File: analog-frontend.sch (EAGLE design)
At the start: 2 parts

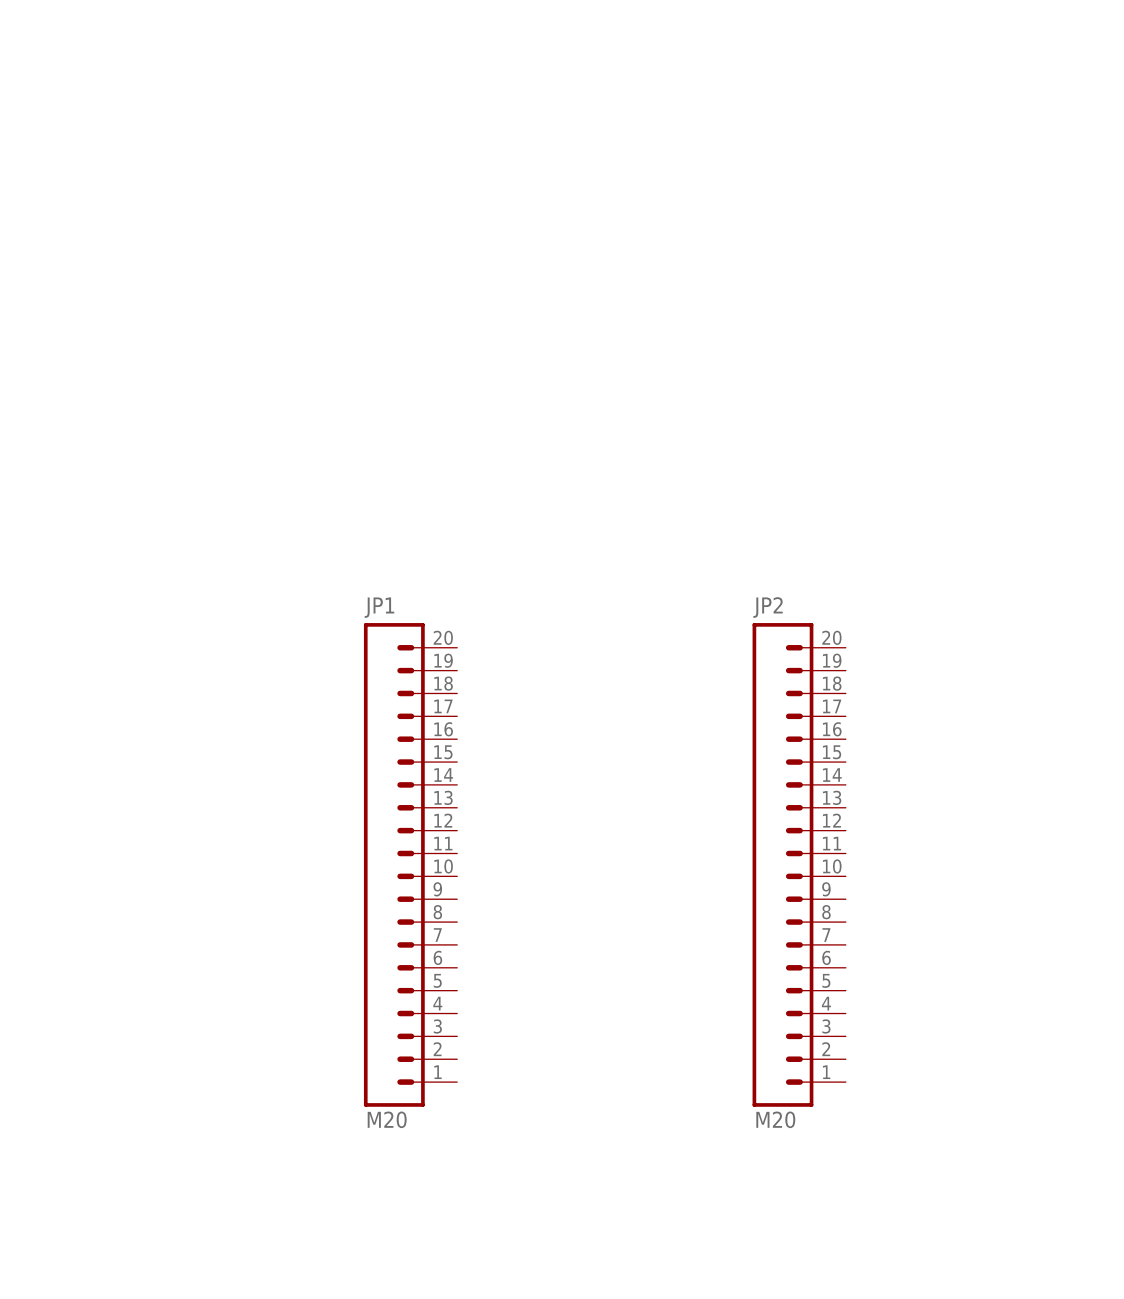
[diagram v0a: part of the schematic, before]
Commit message: added analog mux
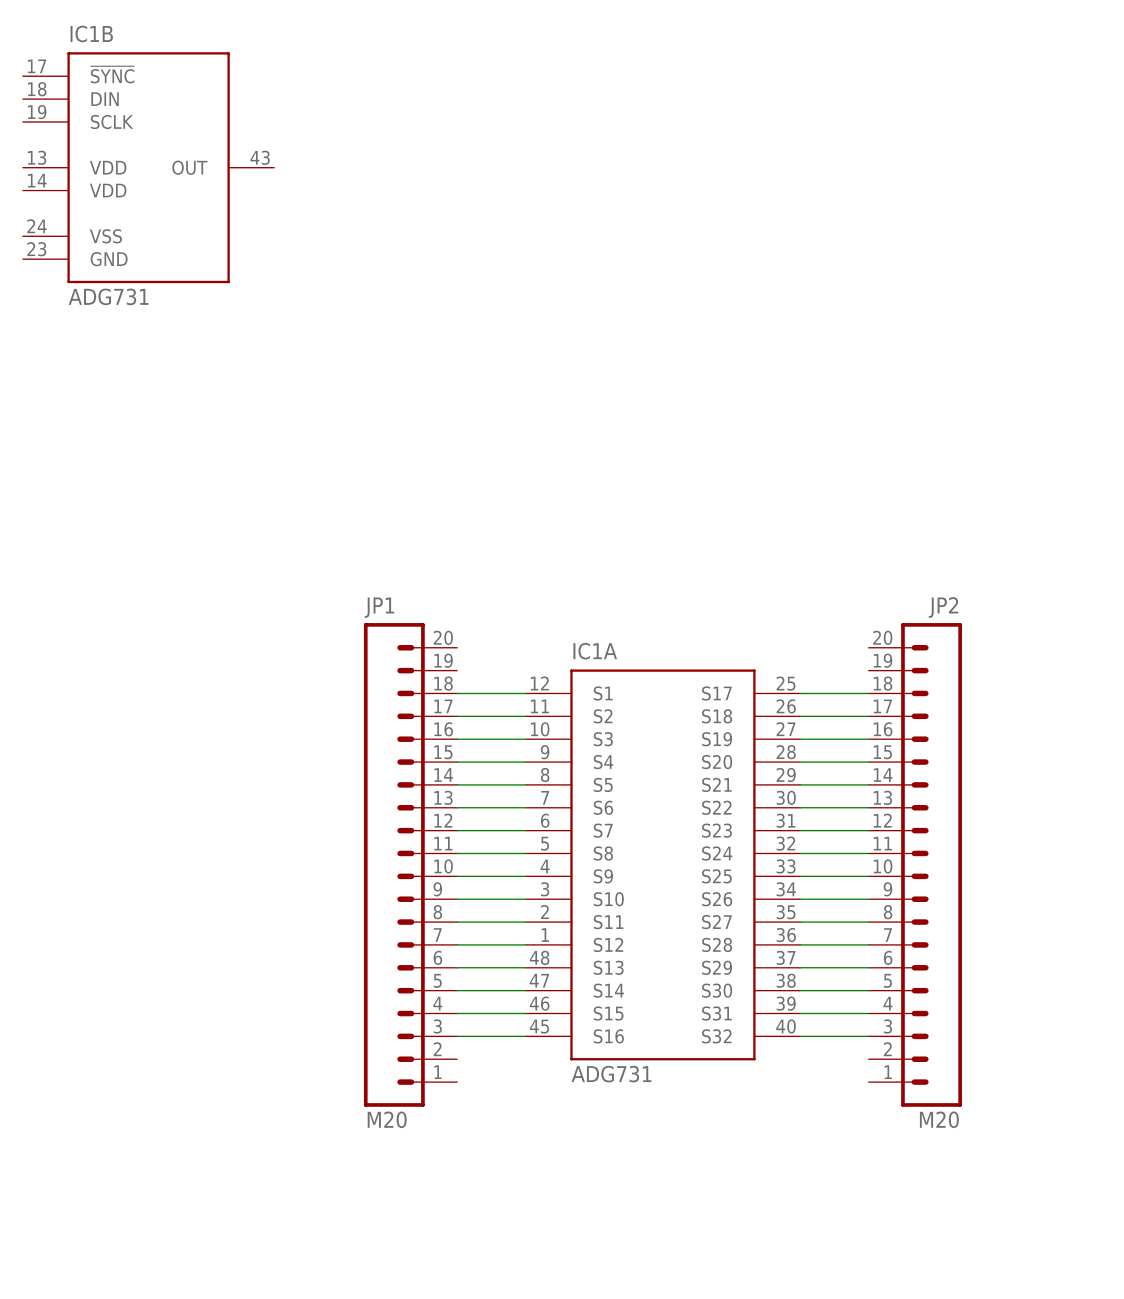
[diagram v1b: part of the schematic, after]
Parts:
- added IC1: ADG731, mor307:ADG731
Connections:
- new net N$1: IC1A.S1, JP1.18
- new net N$10: IC1A.S7, JP1.12
- new net N$11: IC1A.S8, JP1.11
- new net N$12: IC1A.S9, JP1.10
- new net N$13: IC1A.S10, JP1.9
- new net N$14: IC1A.S11, JP1.8
- new net N$15: IC1A.S12, JP1.7
- new net N$16: IC1A.S13, JP1.6
- new net N$17: IC1A.S14, JP1.5
- new net N$18: IC1A.S15, JP1.4
- new net N$19: IC1A.S18, JP2.17
- new net N$2: IC1A.S16, JP1.3
- new net N$20: IC1A.S19, JP2.16
- new net N$21: IC1A.S20, JP2.15
- new net N$22: IC1A.S21, JP2.14
- new net N$23: IC1A.S22, JP2.13
- new net N$24: IC1A.S23, JP2.12
- new net N$25: IC1A.S24, JP2.11
- new net N$26: IC1A.S25, JP2.10
- new net N$27: IC1A.S26, JP2.9
- new net N$28: IC1A.S27, JP2.8
- new net N$29: IC1A.S28, JP2.7
- new net N$3: IC1A.S17, JP2.18
- new net N$30: IC1A.S29, JP2.6
- new net N$31: IC1A.S30, JP2.5
- new net N$32: IC1A.S31, JP2.4
- new net N$4: IC1A.S32, JP2.3
- new net N$5: IC1A.S2, JP1.17
- new net N$6: IC1A.S3, JP1.16
- new net N$7: IC1A.S4, JP1.15
- new net N$8: IC1A.S5, JP1.14
- new net N$9: IC1A.S6, JP1.13
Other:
- moved on the sheet: JP2
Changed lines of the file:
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@@
 <part name="JP1" library="mor307" deviceset="M20" device=""/>
 <part name="JP2" library="mor307" deviceset="M20" device=""/>
+<part name="IC1" library="mor307" deviceset="ADG731" device=""/>
 </parts>
 <sheets>
@@
 </instance>
 <instance part="JP1" gate="G$1" x="73.66" y="144.78"/>
-<instance part="JP2" gate="G$1" x="116.84" y="144.78"/>
+<instance part="JP2" gate="G$1" x="139.7" y="144.78" rot="MR0"/>
+<instance part="IC1" gate="B" x="48.26" y="220.98"/>
+<instance part="IC1" gate="A" x="106.68" y="142.24"/>
 </instances>
 <busses>
 </busses>
 <nets>
+<net name="N$1" class="0">
+<segment>
+<pinref part="IC1" gate="A" pin="S1"/>
+<pinref part="JP1" gate="G$1" pin="18"/>
+<wire x1="91.44" y1="162.56" x2="83.82" y2="162.56" width="0.1524" layer="91"/>
+</segment>
+</net>
+<net name="N$2" class="0">
+<segment>
+<pinref part="IC1" gate="A" pin="S16"/>
+<pinref part="JP1" gate="G$1" pin="3"/>
+<wire x1="91.44" y1="124.46" x2="83.82" y2="124.46" width="0.1524" layer="91"/>
+</segment>
+</net>
+<net name="N$3" class="0">
+<segment>
+<pinref part="IC1" gate="A" pin="S17"/>
+<pinref part="JP2" gate="G$1" pin="18"/>
+<wire x1="121.92" y1="162.56" x2="129.54" y2="162.56" width="0.1524" layer="91"/>
+</segment>
+</net>
+<net name="N$4" class="0">
+<segment>
+<pinref part="IC1" gate="A" pin="S32"/>
+<pinref part="JP2" gate="G$1" pin="3"/>
+<wire x1="121.92" y1="124.46" x2="129.54" y2="124.46" width="0.1524" layer="91"/>
+</segment>
+</net>
+<net name="N$5" class="0">
+<segment>
+<pinref part="IC1" gate="A" pin="S2"/>
+<pinref part="JP1" gate="G$1" pin="17"/>
+<wire x1="91.44" y1="160.02" x2="83.82" y2="160.02" width="0.1524" layer="91"/>
+</segment>
+</net>
+<net name="N$6" class="0">
+<segment>
+<pinref part="IC1" gate="A" pin="S3"/>
+<pinref part="JP1" gate="G$1" pin="16"/>
+<wire x1="91.44" y1="157.48" x2="83.82" y2="157.48" width="0.1524" layer="91"/>
+</segment>
+</net>
+<net name="N$7" class="0">
+<segment>
+<pinref part="IC1" gate="A" pin="S4"/>
+<pinref part="JP1" gate="G$1" pin="15"/>
+<wire x1="91.44" y1="154.94" x2="83.82" y2="154.94" width="0.1524" layer="91"/>
+</segment>
+</net>
+<net name="N$8" class="0">
+<segment>
+<pinref part="IC1" gate="A" pin="S5"/>
+<pinref part="JP1" gate="G$1" pin="14"/>
+<wire x1="91.44" y1="152.4" x2="83.82" y2="152.4" width="0.1524" layer="91"/>
+</segment>
+</net>
+<net name="N$9" class="0">
+<segment>
+<pinref part="IC1" gate="A" pin="S6"/>
+<pinref part="JP1" gate="G$1" pin="13"/>
+<wire x1="91.44" y1="149.86" x2="83.82" y2="149.86" width="0.1524" layer="91"/>
+</segment>
+</net>
+<net name="N$10" class="0">
+<segment>
+<pinref part="IC1" gate="A" pin="S7"/>
+<pinref part="JP1" gate="G$1" pin="12"/>
+<wire x1="91.44" y1="147.32" x2="83.82" y2="147.32" width="0.1524" layer="91"/>
+</segment>
+</net>
+<net name="N$11" class="0">
+<segment>
+<pinref part="IC1" gate="A" pin="S8"/>
+<pinref part="JP1" gate="G$1" pin="11"/>
+<wire x1="91.44" y1="144.78" x2="83.82" y2="144.78" width="0.1524" layer="91"/>
+</segment>
+</net>
+<net name="N$12" class="0">
+<segment>
+<pinref part="IC1" gate="A" pin="S9"/>
+<pinref part="JP1" gate="G$1" pin="10"/>
+<wire x1="91.44" y1="142.24" x2="83.82" y2="142.24" width="0.1524" layer="91"/>
+</segment>
+</net>
+<net name="N$13" class="0">
+<segment>
+<pinref part="IC1" gate="A" pin="S10"/>
+<pinref part="JP1" gate="G$1" pin="9"/>
+<wire x1="91.44" y1="139.7" x2="83.82" y2="139.7" width="0.1524" layer="91"/>
+</segment>
+</net>
+<net name="N$14" class="0">
+<segment>
+<pinref part="IC1" gate="A" pin="S11"/>
+<pinref part="JP1" gate="G$1" pin="8"/>
+<wire x1="91.44" y1="137.16" x2="83.82" y2="137.16" width="0.1524" layer="91"/>
+</segment>
+</net>
+<net name="N$15" class="0">
+<segment>
+<pinref part="IC1" gate="A" pin="S12"/>
+<pinref part="JP1" gate="G$1" pin="7"/>
+<wire x1="91.44" y1="134.62" x2="83.82" y2="134.62" width="0.1524" layer="91"/>
+</segment>
+</net>
+<net name="N$16" class="0">
+<segment>
+<pinref part="IC1" gate="A" pin="S13"/>
+<pinref part="JP1" gate="G$1" pin="6"/>
+<wire x1="91.44" y1="132.08" x2="83.82" y2="132.08" width="0.1524" layer="91"/>
+</segment>
+</net>
+<net name="N$17" class="0">
+<segment>
+<pinref part="IC1" gate="A" pin="S14"/>
+<pinref part="JP1" gate="G$1" pin="5"/>
+<wire x1="91.44" y1="129.54" x2="83.82" y2="129.54" width="0.1524" layer="91"/>
+</segment>
+</net>
+<net name="N$18" class="0">
+<segment>
+<pinref part="IC1" gate="A" pin="S15"/>
+<pinref part="JP1" gate="G$1" pin="4"/>
+<wire x1="91.44" y1="127" x2="83.82" y2="127" width="0.1524" layer="91"/>
+</segment>
+</net>
+<net name="N$19" class="0">
+<segment>
+<pinref part="IC1" gate="A" pin="S18"/>
+<pinref part="JP2" gate="G$1" pin="17"/>
+<wire x1="121.92" y1="160.02" x2="129.54" y2="160.02" width="0.1524" layer="91"/>
+</segment>
+</net>
+<net name="N$20" class="0">
+<segment>
+<pinref part="IC1" gate="A" pin="S19"/>
+<pinref part="JP2" gate="G$1" pin="16"/>
+<wire x1="121.92" y1="157.48" x2="129.54" y2="157.48" width="0.1524" layer="91"/>
+</segment>
+</net>
+<net name="N$21" class="0">
+<segment>
+<pinref part="IC1" gate="A" pin="S20"/>
+<pinref part="JP2" gate="G$1" pin="15"/>
+<wire x1="121.92" y1="154.94" x2="129.54" y2="154.94" width="0.1524" layer="91"/>
+</segment>
+</net>
+<net name="N$22" class="0">
+<segment>
+<pinref part="IC1" gate="A" pin="S21"/>
+<pinref part="JP2" gate="G$1" pin="14"/>
+<wire x1="121.92" y1="152.4" x2="129.54" y2="152.4" width="0.1524" layer="91"/>
+</segment>
+</net>
+<net name="N$23" class="0">
+<segment>
+<pinref part="IC1" gate="A" pin="S22"/>
+<pinref part="JP2" gate="G$1" pin="13"/>
+<wire x1="121.92" y1="149.86" x2="129.54" y2="149.86" width="0.1524" layer="91"/>
+</segment>
+</net>
+<net name="N$24" class="0">
+<segment>
+<pinref part="IC1" gate="A" pin="S23"/>
+<pinref part="JP2" gate="G$1" pin="12"/>
+<wire x1="121.92" y1="147.32" x2="129.54" y2="147.32" width="0.1524" layer="91"/>
+</segment>
+</net>
+<net name="N$25" class="0">
+<segment>
+<pinref part="IC1" gate="A" pin="S24"/>
+<pinref part="JP2" gate="G$1" pin="11"/>
+<wire x1="121.92" y1="144.78" x2="129.54" y2="144.78" width="0.1524" layer="91"/>
+</segment>
+</net>
+<net name="N$26" class="0">
+<segment>
+<pinref part="IC1" gate="A" pin="S25"/>
+<pinref part="JP2" gate="G$1" pin="10"/>
+<wire x1="121.92" y1="142.24" x2="129.54" y2="142.24" width="0.1524" layer="91"/>
+</segment>
+</net>
+<net name="N$27" class="0">
+<segment>
+<pinref part="IC1" gate="A" pin="S26"/>
+<pinref part="JP2" gate="G$1" pin="9"/>
+<wire x1="121.92" y1="139.7" x2="129.54" y2="139.7" width="0.1524" layer="91"/>
+</segment>
+</net>
+<net name="N$28" class="0">
+<segment>
+<pinref part="IC1" gate="A" pin="S27"/>
+<pinref part="JP2" gate="G$1" pin="8"/>
+<wire x1="121.92" y1="137.16" x2="129.54" y2="137.16" width="0.1524" layer="91"/>
+</segment>
+</net>
+<net name="N$29" class="0">
+<segment>
+<pinref part="IC1" gate="A" pin="S28"/>
+<pinref part="JP2" gate="G$1" pin="7"/>
+<wire x1="121.92" y1="134.62" x2="129.54" y2="134.62" width="0.1524" layer="91"/>
+</segment>
+</net>
+<net name="N$30" class="0">
+<segment>
+<pinref part="IC1" gate="A" pin="S29"/>
+<pinref part="JP2" gate="G$1" pin="6"/>
+<wire x1="121.92" y1="132.08" x2="129.54" y2="132.08" width="0.1524" layer="91"/>
+</segment>
+</net>
+<net name="N$31" class="0">
+<segment>
+<pinref part="IC1" gate="A" pin="S30"/>
+<pinref part="JP2" gate="G$1" pin="5"/>
+<wire x1="121.92" y1="129.54" x2="129.54" y2="129.54" width="0.1524" layer="91"/>
+</segment>
+</net>
+<net name="N$32" class="0">
+<segment>
+<pinref part="IC1" gate="A" pin="S31"/>
+<pinref part="JP2" gate="G$1" pin="4"/>
+<wire x1="121.92" y1="127" x2="129.54" y2="127" width="0.1524" layer="91"/>
+</segment>
+</net>
 </nets>
 </sheet>
